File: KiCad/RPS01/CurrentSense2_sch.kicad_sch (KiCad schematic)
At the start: 4 parts

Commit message: Getting THERE. ALMOST THERE
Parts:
- removed R?: 0.2, Resistor_SMD:R_1206_3216Metric, symbol Device:R
- added TP?: VSHUNT2+, Mechatronics TestP:CONN1_RCU-0C_TEC, symbol Connector:TestPoint_Probe
- added TP?: VSHUNT2-, Mechatronics TestP:CONN1_RCU-0C_TEC, symbol Connector:TestPoint_Probe
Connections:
- net LOAD: now also TP?.1, TP?.1
- no-connect marks 5 -> 3
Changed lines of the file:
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@@
 (kicad_sch (version 20230121) (generator eeschema)
   (paper "A4")
+  (junction (at 128.524 49.53) (diameter 0) (color 0 0 0 0)
+  )
   (junction (at 147.574 124.46) (diameter 0) (color 0 0 0 0)
   )
+  (junction (at 139.7 49.53) (diameter 0) (color 0 0 0 0)
+  )
   (junction (at 137.414 141.7826) (diameter 0) (color 0 0 0 0)
   )
@@
   (junction (at 121.412 59.944) (diameter 0) (color 0 0 0 0)
   )
-  (no_connect (at 137.922 45.974))
   (no_connect (at 127.254 122.174))
   (no_connect (at 129.794 66.294))
   (no_connect (at 132.334 122.174))
-  (no_connect (at 130.302 45.974))
   (wire (pts (xy 128.524 59.944) (xy 129.794 59.944))
     (stroke (width 0) (type default))
@@
     (stroke (width 0) (type default))
   )
+  (wire (pts (xy 139.7 49.53) (xy 139.7 59.944))
+    (stroke (width 0) (type default))
+  )
+  (wire (pts (xy 128.524 49.53) (xy 139.7 49.53))
+    (stroke (width 0) (type default))
+  )
   (wire (pts (xy 137.414 125.9998) (xy 147.574 125.9998))
     (stroke (width 0) (type default))
   )
-  (wire (pts (xy 128.524 48.006) (xy 139.7 48.006))
-    (stroke (width 0) (type default))
-  )
   (wire (pts (xy 129.794 122.174) (xy 129.794 125.984))
     (stroke (width 0) (type default))
@@
     (stroke (width 0) (type default))
   )
+  (wire (pts (xy 128.524 49.53) (xy 128.524 48.006))
+    (stroke (width 0) (type default))
+  )
   (wire (pts (xy 147.574 124.46) (xy 159.004 124.46))
     (stroke (width 0) (type default))
@@
     (stroke (width 0) (type default))
   )
-  (wire (pts (xy 128.524 59.944) (xy 128.524 48.006))
+  (wire (pts (xy 128.524 59.944) (xy 128.524 49.53))
     (stroke (width 0) (type default))
   )
@@
     (stroke (width 0) (type default))
   )
-  (wire (pts (xy 139.7 48.006) (xy 139.7 59.944))
+  (wire (pts (xy 139.7 48.006) (xy 139.7 49.53))
     (stroke (width 0) (type default))
   )
@@
         (path "/14930f15-c0a0-4b55-93e6-b112548415f6/83d3dc76-6aeb-422d-8708-14a32de244f0"
           (reference "R31") (unit 1)
+        )
+      )
+    )
+  )
+  (symbol (lib_id "Connector:TestPoint_Probe") (at 128.524 48.006 0) (unit 1)
+    (in_bom yes) (on_board yes) (dnp no)
+    (property "Reference" "TP?" (at 126.492 40.64 0)
+      (effects (font (size 1.27 1.27)) (justify left))
+    )
+    (property "Value" "VSHUNT2+" (at 125.222 42.672 0)
+      (effects (font (size 1.27 1.27)) (justify left))
+    )
+    (property "Footprint" "Mechatronics TestP:CONN1_RCU-0C_TEC" (at 133.604 48.006 0)
+      (effects (font (size 1.27 1.27)) hide)
+    )
+    (property "Datasheet" "~" (at 133.604 48.006 0)
+      (effects (font (size 1.27 1.27)) hide)
+    )
+    (pin "1")
+    (instances
+      (project "rps01"
+        (path "/14930f15-c0a0-4b55-93e6-b112548415f6/577d3fc4-735f-4981-a3a1-4300f23b9ae6"
+          (reference "TP?") (unit 1)
+        )
+        (path "/14930f15-c0a0-4b55-93e6-b112548415f6/13e150ee-6c46-47a5-9c09-3749eb0dcbfe"
+          (reference "TP2") (unit 1)
+        )
+        (path "/14930f15-c0a0-4b55-93e6-b112548415f6/83d3dc76-6aeb-422d-8708-14a32de244f0"
+          (reference "TP12") (unit 1)
+        )
+      )
+    )
+  )
+  (symbol (lib_id "Connector:TestPoint_Probe") (at 139.7 48.006 0) (unit 1)
+    (in_bom yes) (on_board yes) (dnp no) (fields_autoplaced)
+    (property "Reference" "TP?" (at 143.764 45.7835 0)
+      (effects (font (size 1.27 1.27)) (justify left))
+    )
+    (property "Value" "VSHUNT2-" (at 143.764 48.3235 0)
+      (effects (font (size 1.27 1.27)) (justify left))
+    )
+    (property "Footprint" "Mechatronics TestP:CONN1_RCU-0C_TEC" (at 144.78 48.006 0)
+      (effects (font (size 1.27 1.27)) hide)
+    )
+    (property "Datasheet" "~" (at 144.78 48.006 0)
+      (effects (font (size 1.27 1.27)) hide)
+    )
+    (pin "1")
+    (instances
+      (project "rps01"
+        (path "/14930f15-c0a0-4b55-93e6-b112548415f6/577d3fc4-735f-4981-a3a1-4300f23b9ae6"
+          (reference "TP?") (unit 1)
+        )
+        (path "/14930f15-c0a0-4b55-93e6-b112548415f6/13e150ee-6c46-47a5-9c09-3749eb0dcbfe"
+          (reference "TP1") (unit 1)
+        )
+        (path "/14930f15-c0a0-4b55-93e6-b112548415f6/83d3dc76-6aeb-422d-8708-14a32de244f0"
+          (reference "TP11") (unit 1)
         )
       )
@@
         )
       )
-    )
-  )
-  (symbol (lib_id "Device:R") (at 134.112 45.974 90) (unit 1)
-    (in_bom yes) (on_board yes) (dnp no)
-    (property "Reference" "R?" (at 134.112 41.148 90)
-      (effects (font (size 1.27 1.27)))
-    )
-    (property "Value" "0.2" (at 133.858 43.688 90)
-      (effects (font (size 1.27 1.27)))
-    )
-    (property "Footprint" "Resistor_SMD:R_1206_3216Metric" (at 134.112 47.752 90)
-      (effects (font (size 1.27 1.27)) hide)
-    )
-    (property "Datasheet" "~" (at 134.112 45.974 0)
-      (effects (font (size 1.27 1.27)) hide)
-    )
-    (pin "1")
-    (pin "2")
-    (instances
-      (project "rps01"
-        (path "/14930f15-c0a0-4b55-93e6-b112548415f6/13e150ee-6c46-47a5-9c09-3749eb0dcbfe"
-          (reference "R?") (unit 1)
-        )
-        (path "/14930f15-c0a0-4b55-93e6-b112548415f6/83d3dc76-6aeb-422d-8708-14a32de244f0"
-          (reference "R_S4") (unit 1)
-        )
-      )

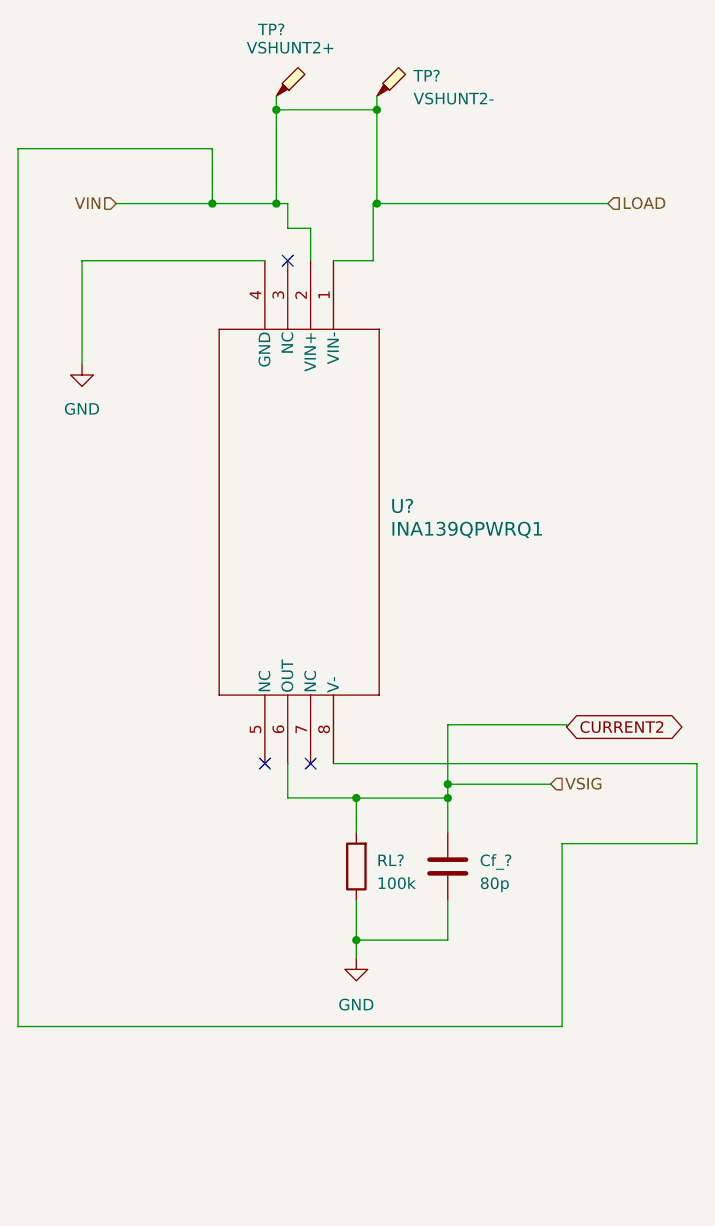
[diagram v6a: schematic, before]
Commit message: add V+ filter caps to current sense schematic
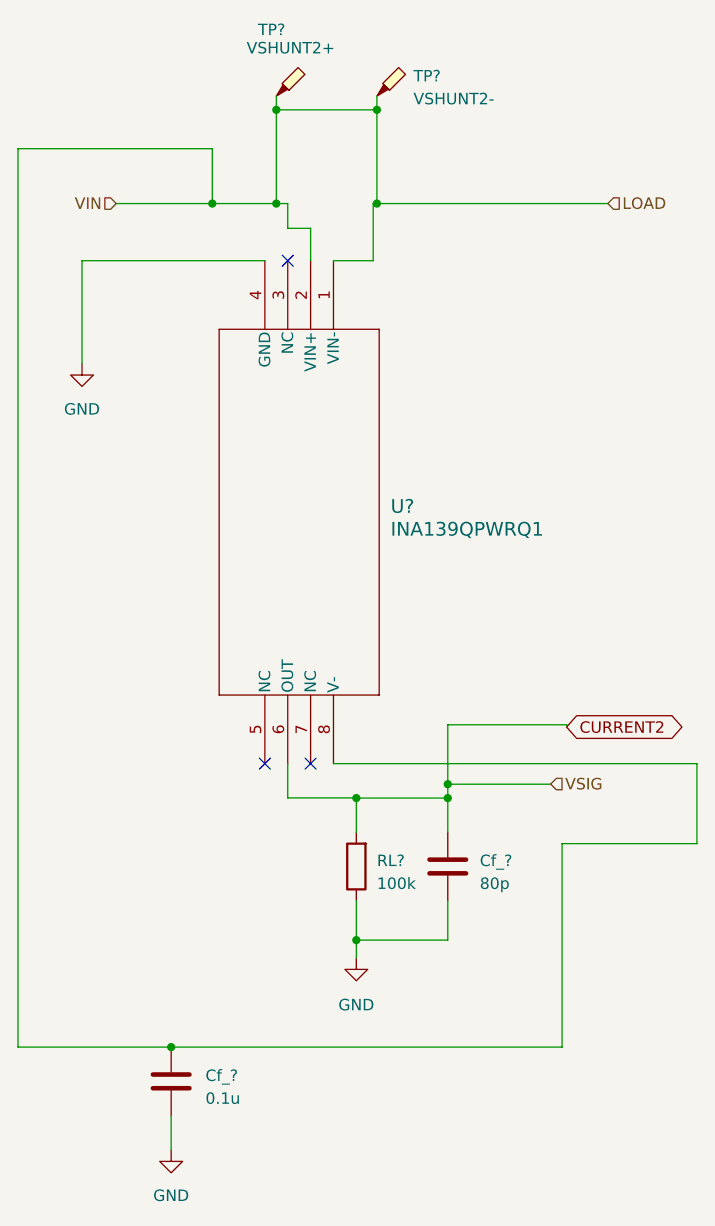
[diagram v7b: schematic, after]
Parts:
- added Cf_?: 0.1u, Capacitor_SMD:C_0603_1608Metric, symbol Device:C
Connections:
- net GND: now also Cf_?.2
- net LOAD: now also Cf_?.1
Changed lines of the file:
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@@
   (junction (at 128.524 49.53) (diameter 0) (color 0 0 0 0)
+  )
+  (junction (at 116.84 153.67) (diameter 0) (color 0 0 0 0)
   )
   (junction (at 147.574 124.46) (diameter 0) (color 0 0 0 0)
@@
     (stroke (width 0) (type default))
   )
-  (wire (pts (xy 99.822 151.384) (xy 99.822 53.848))
+  (wire (pts (xy 99.822 53.848) (xy 99.822 153.67))
     (stroke (width 0) (type default))
   )
@@
     (stroke (width 0) (type default))
   )
+  (wire (pts (xy 99.822 153.67) (xy 116.84 153.67))
+    (stroke (width 0) (type default))
+  )
   (wire (pts (xy 129.794 122.174) (xy 129.794 125.984))
     (stroke (width 0) (type default))
   )
-  (wire (pts (xy 160.274 151.384) (xy 99.822 151.384))
-    (stroke (width 0) (type default))
-  )
   (wire (pts (xy 175.26 131.064) (xy 160.274 131.064))
     (stroke (width 0) (type default))
@@
     (stroke (width 0) (type default))
   )
-  (wire (pts (xy 160.274 131.064) (xy 160.274 151.384))
-    (stroke (width 0) (type default))
-  )
   (wire (pts (xy 139.2882 59.944) (xy 139.2882 66.294))
     (stroke (width 0) (type default))
@@
     (stroke (width 0) (type default))
   )
+  (wire (pts (xy 116.84 161.29) (xy 116.84 165.1))
+    (stroke (width 0) (type default))
+  )
+  (wire (pts (xy 116.84 153.67) (xy 160.274 153.67))
+    (stroke (width 0) (type default))
+  )
   (wire (pts (xy 134.874 122.174) (xy 175.26 122.174))
     (stroke (width 0) (type default))
@@
   )
   (wire (pts (xy 139.7 48.006) (xy 139.7 49.53))
+    (stroke (width 0) (type default))
+  )
+  (wire (pts (xy 160.274 131.064) (xy 160.274 153.67))
     (stroke (width 0) (type default))
   )
@@
         (path "/14930f15-c0a0-4b55-93e6-b112548415f6/83d3dc76-6aeb-422d-8708-14a32de244f0"
           (reference "TP11") (unit 1)
+        )
+      )
+    )
+  )
+  (symbol (lib_id "power:GND") (at 116.84 165.1 0) (unit 1)
+    (in_bom yes) (on_board yes) (dnp no) (fields_autoplaced)
+    (property "Reference" "#PWR092" (at 116.84 171.45 0)
+      (effects (font (size 1.27 1.27)) hide)
+    )
+    (property "Value" "GND" (at 116.84 170.18 0)
+      (effects (font (size 1.27 1.27)))
+    )
+    (property "Footprint" "" (at 116.84 165.1 0)
+      (effects (font (size 1.27 1.27)) hide)
+    )
+    (property "Datasheet" "" (at 116.84 165.1 0)
+      (effects (font (size 1.27 1.27)) hide)
+    )
+    (pin "1")
+    (instances
+      (project "rps01"
+        (path "/14930f15-c0a0-4b55-93e6-b112548415f6/83d3dc76-6aeb-422d-8708-14a32de244f0"
+          (reference "#PWR092") (unit 1)
         )
       )
@@
         )
       )
+    )
+  )
+  (symbol (lib_id "Device:C") (at 116.84 157.48 0) (unit 1)
+    (in_bom yes) (on_board yes) (dnp no) (fields_autoplaced)
+    (property "Reference" "Cf_?" (at 120.65 156.845 0)
+      (effects (font (size 1.27 1.27)) (justify left))
+    )
+    (property "Value" "0.1u" (at 120.65 159.385 0)
+      (effects (font (size 1.27 1.27)) (justify left))
+    )
+    (property "Footprint" "Capacitor_SMD:C_0603_1608Metric" (at 117.8052 161.29 0)
+      (effects (font (size 1.27 1.27)) hide)
+    )
+    (property "Datasheet" "~" (at 116.84 157.48 0)
+      (effects (font (size 1.27 1.27)) hide)
+    )
+    (pin "1")
+    (pin "2")
+    (instances
+      (project "rps01"
+        (path "/14930f15-c0a0-4b55-93e6-b112548415f6/13e150ee-6c46-47a5-9c09-3749eb0dcbfe"
+          (reference "Cf_?") (unit 1)
+        )
+        (path "/14930f15-c0a0-4b55-93e6-b112548415f6/83d3dc76-6aeb-422d-8708-14a32de244f0"
+          (reference "Cf_1") (unit 1)
+        )
+      )
